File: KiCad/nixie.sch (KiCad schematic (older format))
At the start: 13 parts

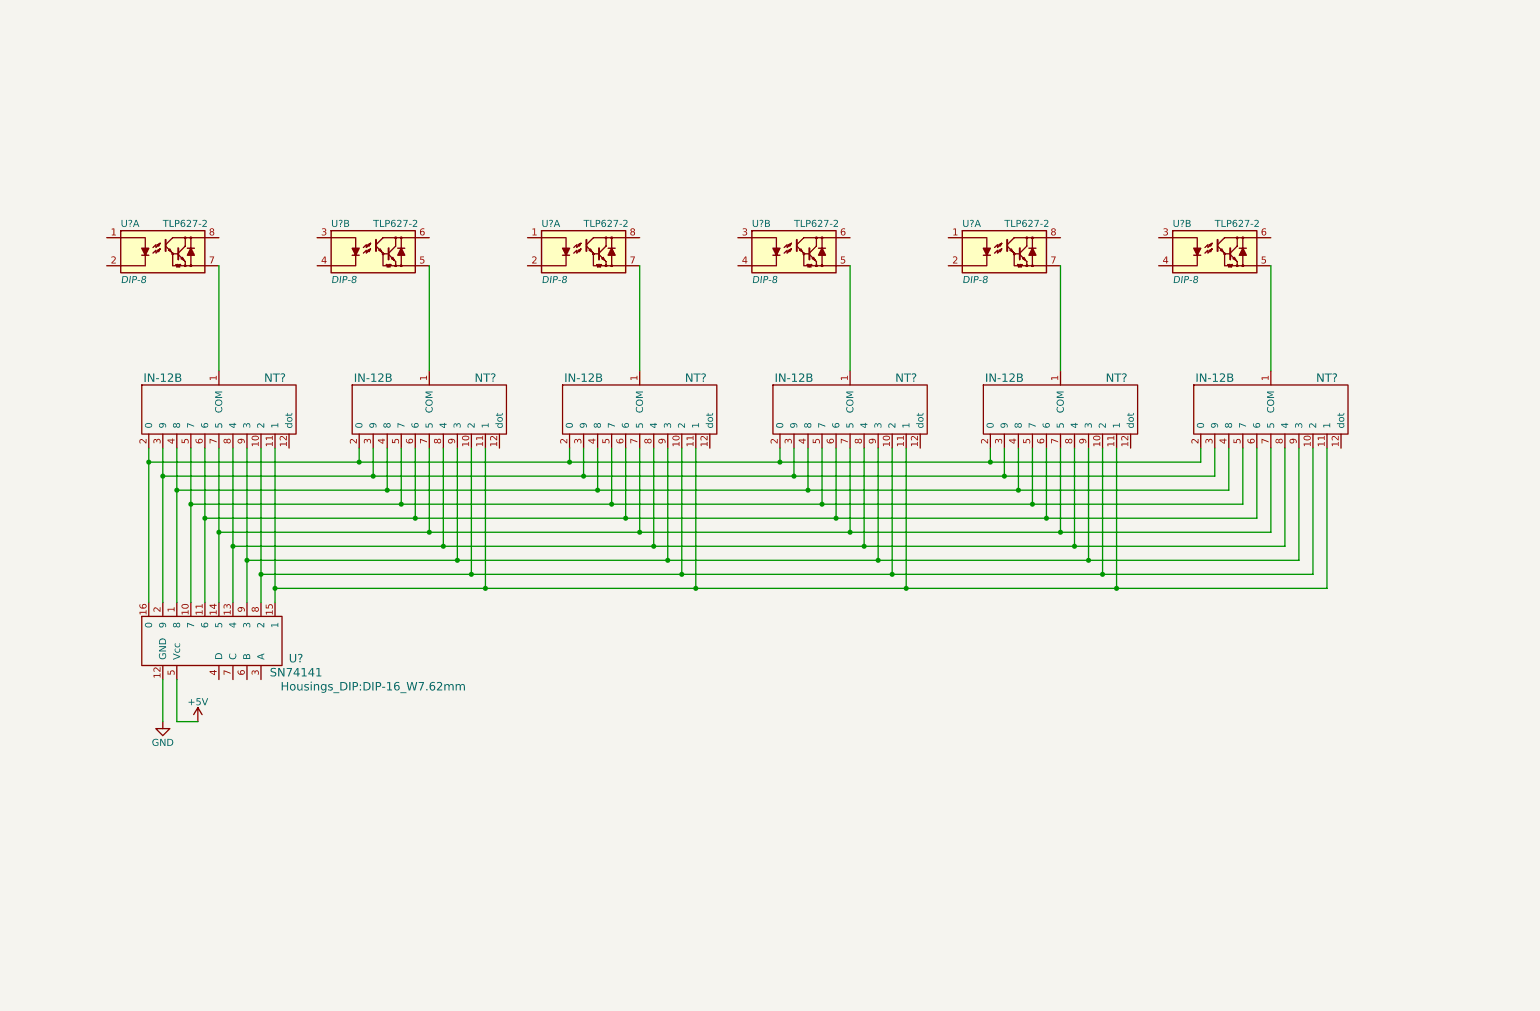
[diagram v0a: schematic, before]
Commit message: add power schematic
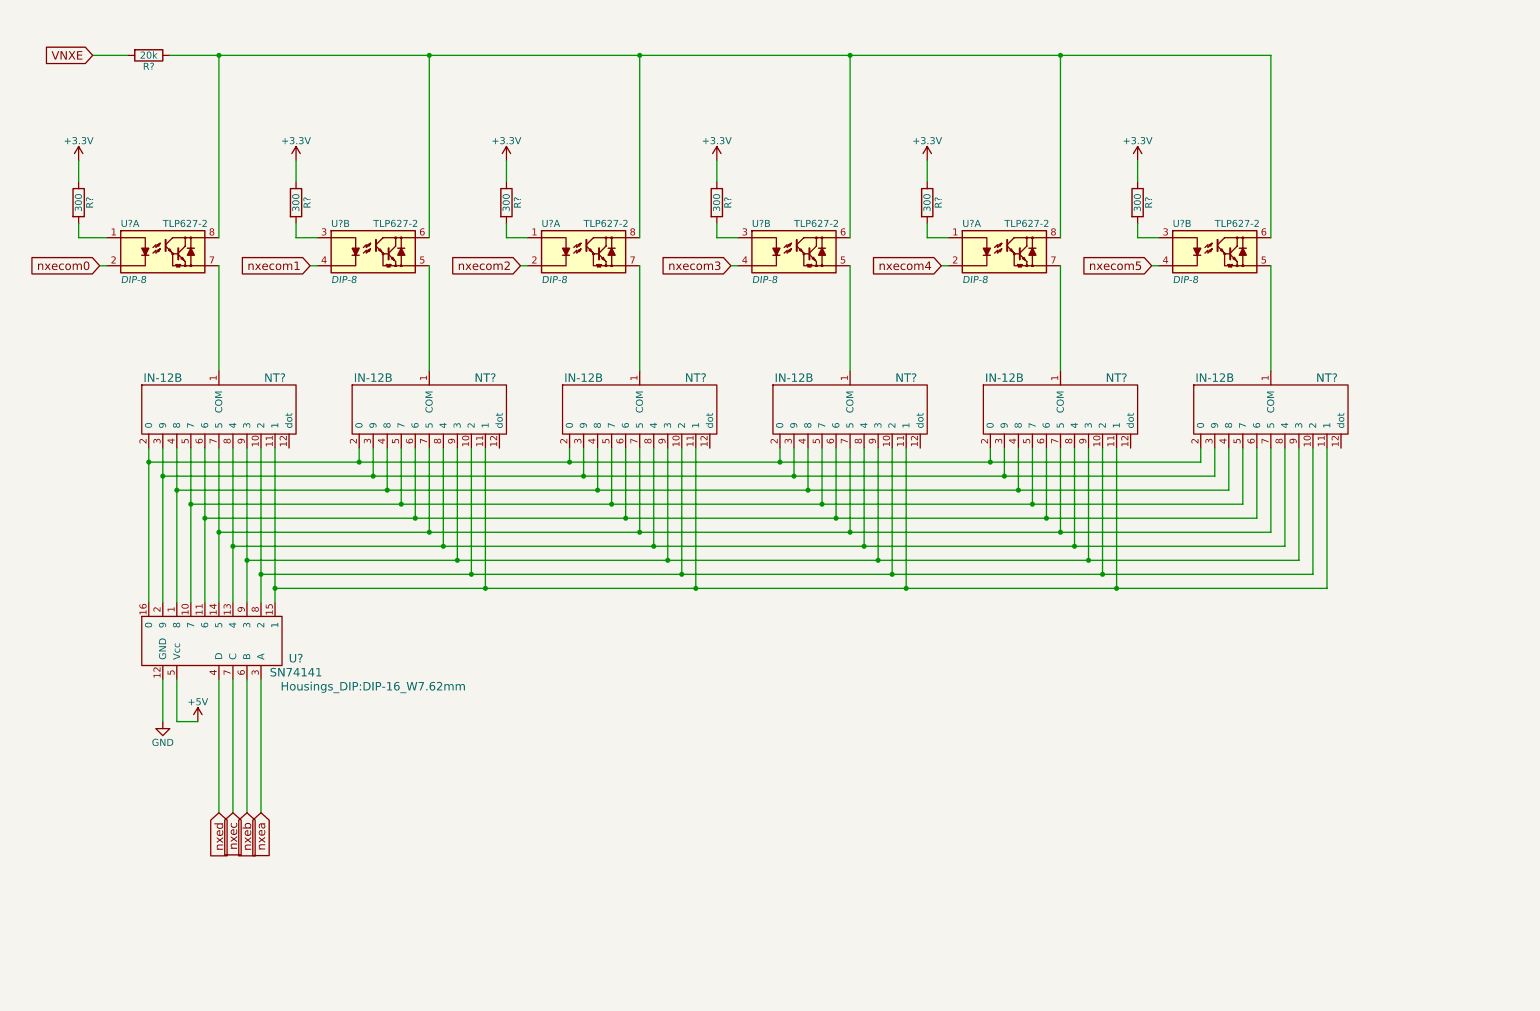
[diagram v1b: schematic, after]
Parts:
- added R? (x6): 300, symbol R
- added R?: 20k, symbol R
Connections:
- net at U?.1: now also R?.2 (x3)
- net nxecom0: now reaches U?.2
- net at U?.8: now also U?.6, U?.6, U?.6, U?.8, U?.8, R?.1
- net at U?.3: now also R?.2 (x3)
- net nxecom1: now reaches U?.4
- net nxecom2: now reaches U?.2
- net nxecom3: now reaches U?.4
- net nxecom4: now reaches U?.2
- net nxecom5: now reaches U?.4
- net nxea: now reaches U?.3 (A)
- net nxed: now reaches U?.4 (D)
- net nxeb: now reaches U?.6 (B)
- net nxec: now reaches U?.7 (C)
- new net +3V3: R?.1, R?.1, R?.1, R?.1, R?.1, R?.1
- new net VNXE: R?.2

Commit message: change schematics
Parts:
- gave numbers to parts that had none: 17
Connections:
- no-connect marks 0 -> 6
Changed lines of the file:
@@
 $EndDescr
 $Comp
-L IN-12B NT?
+L IN-12B NT1
 U 1 1 59E23BBC
 P 1700 3700
-F 0 "NT?" H 2300 4100 60  0000 C CNN
+F 0 "NT1" H 2300 4100 60  0000 C CNN
 F 1 "IN-12B" H 1500 4100 60  0000 C CNN
 F 2 "" H 1700 3700 60  0000 C CNN
@@
 $EndComp
 $Comp
-L IN-12B NT?
+L IN-12B NT2
 U 1 1 59E23D59
 P 3200 3700
-F 0 "NT?" H 3800 4100 60  0000 C CNN
+F 0 "NT2" H 3800 4100 60  0000 C CNN
 F 1 "IN-12B" H 3000 4100 60  0000 C CNN
 F 2 "" H 3200 3700 60  0000 C CNN
@@
 $EndComp
 $Comp
-L IN-12B NT?
+L IN-12B NT3
 U 1 1 59E23EDD
 P 4700 3700
-F 0 "NT?" H 5300 4100 60  0000 C CNN
+F 0 "NT3" H 5300 4100 60  0000 C CNN
 F 1 "IN-12B" H 4500 4100 60  0000 C CNN
 F 2 "" H 4700 3700 60  0000 C CNN
@@
 $EndComp
 $Comp
-L IN-12B NT?
+L IN-12B NT4
 U 1 1 59E23EE3
 P 6200 3700
-F 0 "NT?" H 6800 4100 60  0000 C CNN
+F 0 "NT4" H 6800 4100 60  0000 C CNN
 F 1 "IN-12B" H 6000 4100 60  0000 C CNN
 F 2 "" H 6200 3700 60  0000 C CNN
@@
 $EndComp
 $Comp
-L IN-12B NT?
+L IN-12B NT5
 U 1 1 59E24011
 P 7700 3700
-F 0 "NT?" H 8300 4100 60  0000 C CNN
+F 0 "NT5" H 8300 4100 60  0000 C CNN
 F 1 "IN-12B" H 7500 4100 60  0000 C CNN
 F 2 "" H 7700 3700 60  0000 C CNN
@@
 $EndComp
 $Comp
-L IN-12B NT?
+L IN-12B NT6
 U 1 1 59E24017
 P 9200 3700
-F 0 "NT?" H 9800 4100 60  0000 C CNN
+F 0 "NT6" H 9800 4100 60  0000 C CNN
 F 1 "IN-12B" H 9000 4100 60  0000 C CNN
 F 2 "" H 9200 3700 60  0000 C CNN
@@
 $EndComp
 $Comp
-L TLP627-2 U?
+L TLP627-2 U2
 U 1 1 59E2402B
 P 1500 2400
-F 0 "U?" H 1200 2600 50  0000 L CNN
+F 0 "U2" H 1200 2600 50  0000 L CNN
 F 1 "TLP627-2" H 1500 2600 50  0000 L CNN
 F 2 "DIP-8" H 1200 2200 50  0000 L CIN
@@
 $EndComp
 $Comp
-L TLP627-2 U?
+L TLP627-2 U2
 U 2 1 59E24124
 P 3000 2400
-F 0 "U?" H 2700 2600 50  0000 L CNN
+F 0 "U2" H 2700 2600 50  0000 L CNN
 F 1 "TLP627-2" H 3000 2600 50  0000 L CNN
 F 2 "DIP-8" H 2700 2200 50  0000 L CIN
@@
 $EndComp
 $Comp
-L TLP627-2 U?
+L TLP627-2 U4
 U 1 1 59E241FF
 P 4500 2400
-F 0 "U?" H 4200 2600 50  0000 L CNN
+F 0 "U4" H 4200 2600 50  0000 L CNN
 F 1 "TLP627-2" H 4500 2600 50  0000 L CNN
 F 2 "DIP-8" H 4200 2200 50  0000 L CIN
@@
 $EndComp
 $Comp
-L TLP627-2 U?
+L TLP627-2 U4
 U 2 1 59E24205
 P 6000 2400
-F 0 "U?" H 5700 2600 50  0000 L CNN
+F 0 "U4" H 5700 2600 50  0000 L CNN
 F 1 "TLP627-2" H 6000 2600 50  0000 L CNN
 F 2 "DIP-8" H 5700 2200 50  0000 L CIN
@@
 $EndComp
 $Comp
-L TLP627-2 U?
+L TLP627-2 U5
 U 1 1 59E24315
 P 7500 2400
-F 0 "U?" H 7200 2600 50  0000 L CNN
+F 0 "U5" H 7200 2600 50  0000 L CNN
 F 1 "TLP627-2" H 7500 2600 50  0000 L CNN
 F 2 "DIP-8" H 7200 2200 50  0000 L CIN
@@
 $EndComp
 $Comp
-L TLP627-2 U?
+L TLP627-2 U5
 U 2 1 59E2431B
 P 9000 2400
-F 0 "U?" H 8700 2600 50  0000 L CNN
+F 0 "U5" H 8700 2600 50  0000 L CNN
 F 1 "TLP627-2" H 9000 2600 50  0000 L CNN
 F 2 "DIP-8" H 8700 2200 50  0000 L CIN
@@
 $EndComp
 $Comp
-L SN74141 U?
+L SN74141 U3
 U 1 1 59E264B9
 P 1750 5050
-F 0 "U?" H 2450 4800 60  0000 C CNN
+F 0 "U3" H 2450 4800 60  0000 C CNN
 F 1 "SN74141" H 2450 4700 60  0000 C CNN
 F 2 "Housings_DIP:DIP-16_W7.62mm" H 3000 4600 60  0000 C CNN
@@
 	9400 2500 9400 3250
 $Comp
-L GND #PWR01
+L GND #PWR05
 U 1 1 59E29123
 P 1500 5750
-F 0 "#PWR01" H 1500 5500 50  0001 C CNN
+F 0 "#PWR05" H 1500 5500 50  0001 C CNN
 F 1 "GND" H 1500 5600 50  0000 C CNN
 F 2 "" H 1500 5750 50  0000 C CNN
@@
 	1500 5450 1500 5750
 $Comp
-L +5V #PWR02
+L +5V #PWR06
 U 1 1 59E291DF
 P 1750 5750
-F 0 "#PWR02" H 1750 5600 50  0001 C CNN
+F 0 "#PWR06" H 1750 5600 50  0001 C CNN
 F 1 "+5V" H 1750 5890 50  0000 C CNN
 F 2 "" H 1750 5750 50  0000 C CNN
@@
 	1600 5750 1750 5750
 $Comp
-L R R?
+L R R1
 U 1 1 59E47517
 P 900 2050
-F 0 "R?" V 980 2050 50  0000 C CNN
+F 0 "R1" V 980 2050 50  0000 C CNN
 F 1 "300" V 900 2050 50  0000 C CNN
 F 2 "" V 830 2050 50  0000 C CNN
@@
 $EndComp
 $Comp
-L R R?
+L R R3
 U 1 1 59E47712
 P 2450 2050
-F 0 "R?" V 2530 2050 50  0000 C CNN
+F 0 "R3" V 2530 2050 50  0000 C CNN
 F 1 "300" V 2450 2050 50  0000 C CNN
 F 2 "" V 2380 2050 50  0000 C CNN
@@
 $EndComp
 $Comp
-L R R?
+L R R4
 U 1 1 59E47834
 P 3950 2050
-F 0 "R?" V 4030 2050 50  0000 C CNN
+F 0 "R4" V 4030 2050 50  0000 C CNN
 F 1 "300" V 3950 2050 50  0000 C CNN
 F 2 "" V 3880 2050 50  0000 C CNN
@@
 $EndComp
 $Comp
-L R R?
+L R R5
 U 1 1 59E4786D
 P 5450 2050
-F 0 "R?" V 5530 2050 50  0000 C CNN
+F 0 "R5" V 5530 2050 50  0000 C CNN
 F 1 "300" V 5450 2050 50  0000 C CNN
 F 2 "" V 5380 2050 50  0000 C CNN
@@
 $EndComp
 $Comp
-L R R?
+L R R6
 U 1 1 59E47F38
 P 6950 2050
-F 0 "R?" V 7030 2050 50  0000 C CNN
+F 0 "R6" V 7030 2050 50  0000 C CNN
 F 1 "300" V 6950 2050 50  0000 C CNN
 F 2 "" V 6880 2050 50  0000 C CNN
@@
 $EndComp
 $Comp
-L R R?
+L R R7
 U 1 1 59E47FC5
 P 8450 2050
-F 0 "R?" V 8530 2050 50  0000 C CNN
+F 0 "R7" V 8530 2050 50  0000 C CNN
 F 1 "300" V 8450 2050 50  0000 C CNN
 F 2 "" V 8380 2050 50  0000 C CNN
@@
 	8450 2300 8600 2300
 $Comp
-L +3.3V #PWR03
+L +3.3V #PWR07
 U 1 1 59E4B3AF
 P 900 1750
-F 0 "#PWR03" H 900 1600 50  0001 C CNN
+F 0 "#PWR07" H 900 1600 50  0001 C CNN
 F 1 "+3.3V" H 900 1890 50  0000 C CNN
 F 2 "" H 900 1750 50  0000 C CNN
@@
 $EndComp
 $Comp
-L +3.3V #PWR04
+L +3.3V #PWR08
 U 1 1 59E4B4A5
 P 2450 1750
-F 0 "#PWR04" H 2450 1600 50  0001 C CNN
+F 0 "#PWR08" H 2450 1600 50  0001 C CNN
 F 1 "+3.3V" H 2450 1890 50  0000 C CNN
 F 2 "" H 2450 1750 50  0000 C CNN
@@
 $EndComp
 $Comp
-L +3.3V #PWR05
+L +3.3V #PWR09
 U 1 1 59E4B5DB
 P 3950 1750
-F 0 "#PWR05" H 3950 1600 50  0001 C CNN
+F 0 "#PWR09" H 3950 1600 50  0001 C CNN
 F 1 "+3.3V" H 3950 1890 50  0000 C CNN
 F 2 "" H 3950 1750 50  0000 C CNN
@@
 $EndComp
 $Comp
-L +3.3V #PWR06
+L +3.3V #PWR010
 U 1 1 59E4B61A
 P 5450 1750
-F 0 "#PWR06" H 5450 1600 50  0001 C CNN
+F 0 "#PWR010" H 5450 1600 50  0001 C CNN
 F 1 "+3.3V" H 5450 1890 50  0000 C CNN
 F 2 "" H 5450 1750 50  0000 C CNN
@@
 $EndComp
 $Comp
-L +3.3V #PWR07
+L +3.3V #PWR011
 U 1 1 59E4B79C
 P 6950 1750
-F 0 "#PWR07" H 6950 1600 50  0001 C CNN
+F 0 "#PWR011" H 6950 1600 50  0001 C CNN
 F 1 "+3.3V" H 6950 1890 50  0000 C CNN
 F 2 "" H 6950 1750 50  0000 C CNN
@@
 $EndComp
 $Comp
-L +3.3V #PWR08
+L +3.3V #PWR012
 U 1 1 59E4B7C8
 P 8450 1750
-F 0 "#PWR08" H 8450 1600 50  0001 C CNN
+F 0 "#PWR012" H 8450 1600 50  0001 C CNN
 F 1 "+3.3V" H 8450 1890 50  0000 C CNN
 F 2 "" H 8450 1750 50  0000 C CNN
@@
 	900  1750 900  1900
 $Comp
-L R R?
+L R R2
 U 1 1 59E4E5A0
 P 1400 1000
-F 0 "R?" V 1480 1000 50  0000 C CNN
+F 0 "R2" V 1480 1000 50  0000 C CNN
 F 1 "20k" V 1400 1000 50  0000 C CNN
 F 2 "" V 1330 1000 50  0000 C CNN
@@
 Text GLabel 1900 6400 3    60   Input ~ 0
 nxed
+NoConn ~ 2400 3800
+NoConn ~ 3900 3800
+NoConn ~ 5400 3800
+NoConn ~ 6900 3800
+NoConn ~ 8400 3800
+NoConn ~ 9900 3800
 $EndSCHEMATC

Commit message: add pcb design
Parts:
- R1, R2, R3, R4, R5, R6, R7: footprint (none) -> Resistors_ThroughHole:R_Axial_DIN0207_L6.3mm_D2.5mm_P10.16mm_Horizontal
- U2, U4, U5: footprint DIP-8 -> Housings_DIP:DIP-8_W7.62mm
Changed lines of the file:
@@
 F 0 "NT1" H 2300 4100 60  0000 C CNN
 F 1 "IN-12B" H 1500 4100 60  0000 C CNN
-F 2 "" H 1700 3700 60  0000 C CNN
+F 2 "" H 1700 3700 60  0001 C CNN
 F 3 "" H 1700 3700 60  0000 C CNN
 	1    1700 3700
@@
 F 0 "NT2" H 3800 4100 60  0000 C CNN
 F 1 "IN-12B" H 3000 4100 60  0000 C CNN
-F 2 "" H 3200 3700 60  0000 C CNN
+F 2 "" H 3200 3700 60  0001 C CNN
 F 3 "" H 3200 3700 60  0000 C CNN
 	1    3200 3700
@@
 F 0 "NT3" H 5300 4100 60  0000 C CNN
 F 1 "IN-12B" H 4500 4100 60  0000 C CNN
-F 2 "" H 4700 3700 60  0000 C CNN
+F 2 "" H 4700 3700 60  0001 C CNN
 F 3 "" H 4700 3700 60  0000 C CNN
 	1    4700 3700
@@
 F 0 "NT4" H 6800 4100 60  0000 C CNN
 F 1 "IN-12B" H 6000 4100 60  0000 C CNN
-F 2 "" H 6200 3700 60  0000 C CNN
+F 2 "" H 6200 3700 60  0001 C CNN
 F 3 "" H 6200 3700 60  0000 C CNN
 	1    6200 3700
@@
 F 0 "NT5" H 8300 4100 60  0000 C CNN
 F 1 "IN-12B" H 7500 4100 60  0000 C CNN
-F 2 "" H 7700 3700 60  0000 C CNN
+F 2 "" H 7700 3700 60  0001 C CNN
 F 3 "" H 7700 3700 60  0000 C CNN
 	1    7700 3700
@@
 F 0 "NT6" H 9800 4100 60  0000 C CNN
 F 1 "IN-12B" H 9000 4100 60  0000 C CNN
-F 2 "" H 9200 3700 60  0000 C CNN
+F 2 "" H 9200 3700 60  0001 C CNN
 F 3 "" H 9200 3700 60  0000 C CNN
 	1    9200 3700
@@
 F 0 "U2" H 1200 2600 50  0000 L CNN
 F 1 "TLP627-2" H 1500 2600 50  0000 L CNN
-F 2 "DIP-8" H 1200 2200 50  0000 L CIN
+F 2 "Housings_DIP:DIP-8_W7.62mm" H 1200 2200 50  0001 L CIN
 F 3 "" H 1500 2400 50  0000 L CNN
 	1    1500 2400
@@
 F 0 "U2" H 2700 2600 50  0000 L CNN
 F 1 "TLP627-2" H 3000 2600 50  0000 L CNN
-F 2 "DIP-8" H 2700 2200 50  0000 L CIN
+F 2 "Housings_DIP:DIP-8_W7.62mm" H 2700 2200 50  0001 L CIN
 F 3 "" H 3000 2400 50  0000 L CNN
 	2    3000 2400
@@
 F 0 "U4" H 4200 2600 50  0000 L CNN
 F 1 "TLP627-2" H 4500 2600 50  0000 L CNN
-F 2 "DIP-8" H 4200 2200 50  0000 L CIN
+F 2 "Housings_DIP:DIP-8_W7.62mm" H 4200 2200 50  0001 L CIN
 F 3 "" H 4500 2400 50  0000 L CNN
 	1    4500 2400
@@
 F 0 "U4" H 5700 2600 50  0000 L CNN
 F 1 "TLP627-2" H 6000 2600 50  0000 L CNN
-F 2 "DIP-8" H 5700 2200 50  0000 L CIN
+F 2 "Housings_DIP:DIP-8_W7.62mm" H 5700 2200 50  0001 L CIN
 F 3 "" H 6000 2400 50  0000 L CNN
 	2    6000 2400
@@
 F 0 "U5" H 7200 2600 50  0000 L CNN
 F 1 "TLP627-2" H 7500 2600 50  0000 L CNN
-F 2 "DIP-8" H 7200 2200 50  0000 L CIN
+F 2 "Housings_DIP:DIP-8_W7.62mm" H 7200 2200 50  0001 L CIN
 F 3 "" H 7500 2400 50  0000 L CNN
 	1    7500 2400
@@
 F 0 "U5" H 8700 2600 50  0000 L CNN
 F 1 "TLP627-2" H 9000 2600 50  0000 L CNN
-F 2 "DIP-8" H 8700 2200 50  0000 L CIN
+F 2 "Housings_DIP:DIP-8_W7.62mm" H 8700 2200 50  0001 L CIN
 F 3 "" H 9000 2400 50  0000 L CNN
 	2    9000 2400
@@
 F 0 "R1" V 980 2050 50  0000 C CNN
 F 1 "300" V 900 2050 50  0000 C CNN
-F 2 "" V 830 2050 50  0000 C CNN
+F 2 "Resistors_ThroughHole:R_Axial_DIN0207_L6.3mm_D2.5mm_P10.16mm_Horizontal" V 830 2050 50  0001 C CNN
 F 3 "" H 900 2050 50  0000 C CNN
 	1    900  2050
@@
 F 0 "R3" V 2530 2050 50  0000 C CNN
 F 1 "300" V 2450 2050 50  0000 C CNN
-F 2 "" V 2380 2050 50  0000 C CNN
+F 2 "Resistors_ThroughHole:R_Axial_DIN0207_L6.3mm_D2.5mm_P10.16mm_Horizontal" V 2380 2050 50  0001 C CNN
 F 3 "" H 2450 2050 50  0000 C CNN
 	1    2450 2050
@@
 F 0 "R4" V 4030 2050 50  0000 C CNN
 F 1 "300" V 3950 2050 50  0000 C CNN
-F 2 "" V 3880 2050 50  0000 C CNN
+F 2 "Resistors_ThroughHole:R_Axial_DIN0207_L6.3mm_D2.5mm_P10.16mm_Horizontal" V 3880 2050 50  0001 C CNN
 F 3 "" H 3950 2050 50  0000 C CNN
 	1    3950 2050
@@
 F 0 "R5" V 5530 2050 50  0000 C CNN
 F 1 "300" V 5450 2050 50  0000 C CNN
-F 2 "" V 5380 2050 50  0000 C CNN
+F 2 "Resistors_ThroughHole:R_Axial_DIN0207_L6.3mm_D2.5mm_P10.16mm_Horizontal" V 5380 2050 50  0001 C CNN
 F 3 "" H 5450 2050 50  0000 C CNN
 	1    5450 2050
@@
 F 0 "R6" V 7030 2050 50  0000 C CNN
 F 1 "300" V 6950 2050 50  0000 C CNN
-F 2 "" V 6880 2050 50  0000 C CNN
+F 2 "Resistors_ThroughHole:R_Axial_DIN0207_L6.3mm_D2.5mm_P10.16mm_Horizontal" V 6880 2050 50  0001 C CNN
 F 3 "" H 6950 2050 50  0000 C CNN
 	1    6950 2050
@@
 F 0 "R7" V 8530 2050 50  0000 C CNN
 F 1 "300" V 8450 2050 50  0000 C CNN
-F 2 "" V 8380 2050 50  0000 C CNN
+F 2 "Resistors_ThroughHole:R_Axial_DIN0207_L6.3mm_D2.5mm_P10.16mm_Horizontal" V 8380 2050 50  0001 C CNN
 F 3 "" H 8450 2050 50  0000 C CNN
 	1    8450 2050
@@
 F 0 "R2" V 1480 1000 50  0000 C CNN
 F 1 "20k" V 1400 1000 50  0000 C CNN
-F 2 "" V 1330 1000 50  0000 C CNN
+F 2 "Resistors_ThroughHole:R_Axial_DIN0207_L6.3mm_D2.5mm_P10.16mm_Horizontal" V 1330 1000 50  0001 C CNN
 F 3 "" H 1400 1000 50  0000 C CNN
 	1    1400 1000
